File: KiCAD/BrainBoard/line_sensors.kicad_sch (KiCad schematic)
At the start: 0 parts

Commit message: feat: Line sensor thing push
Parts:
- added J6, J7, J8, J9: Conn_01x03_Socket, Connector_PinSocket_2.54mm:PinSocket_1x03_P2.54mm_Vertical, symbol Connector:Conn_01x03_Socket
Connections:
- new net 3V3: J6.2 (Pin_2), J7.2 (Pin_2), J8.2 (Pin_2), J9.2 (Pin_2)
- new net GND: J6.3 (Pin_3), J7.3 (Pin_3), J8.3 (Pin_3), J9.3 (Pin_3)
- new net LINE_1: J6.1 (Pin_1)
- new net LINE_2: J7.1 (Pin_1)
- new net LINE_3: J8.1 (Pin_1)
- new net LINE_4: J9.1 (Pin_1)

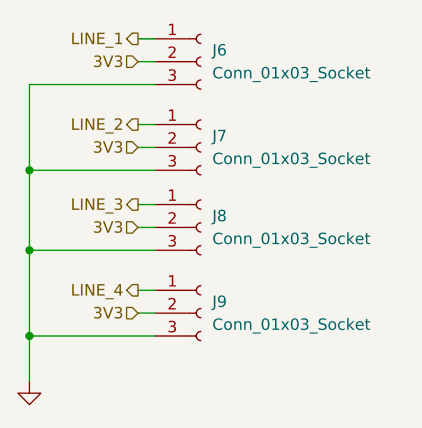
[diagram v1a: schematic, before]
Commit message: feat: add +5V line
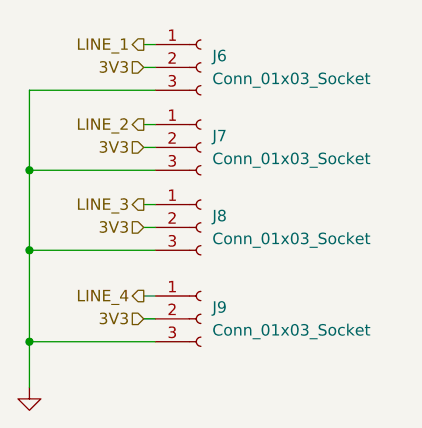
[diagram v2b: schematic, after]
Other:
- moved on the sheet: J6, J9
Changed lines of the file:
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@@
 	)
 	(junction
-		(at 139.7 121.285)
+		(at 139.7 121.92)
 		(diameter 0)
 		(color 0 0 0 0)
@@
 	(wire
 		(pts
-			(xy 151.765 116.205) (xy 153.67 116.205)
-		)
-		(stroke
-			(width 0)
-			(type default)
-		)
-	)
-	(wire
-		(pts
-			(xy 151.765 109.22) (xy 153.67 109.22)
-		)
-		(stroke
-			(width 0)
-			(type default)
-		)
-	)
-	(wire
-		(pts
-			(xy 151.765 88.265) (xy 153.67 88.265)
-		)
-		(stroke
-			(width 0)
-			(type default)
-		)
-	)
-	(wire
-		(pts
-			(xy 151.765 97.79) (xy 153.67 97.79)
-		)
-		(stroke
-			(width 0)
-			(type default)
-		)
-	)
-	(wire
-		(pts
-			(xy 151.765 118.745) (xy 153.67 118.745)
+			(xy 152.4 116.84) (xy 153.67 116.84)
+		)
+		(stroke
+			(width 0)
+			(type default)
+		)
+	)
+	(wire
+		(pts
+			(xy 152.4 109.22) (xy 153.67 109.22)
+		)
+		(stroke
+			(width 0)
+			(type default)
+		)
+	)
+	(wire
+		(pts
+			(xy 152.4 88.9) (xy 153.67 88.9)
+		)
+		(stroke
+			(width 0)
+			(type default)
+		)
+	)
+	(wire
+		(pts
+			(xy 152.4 97.79) (xy 153.67 97.79)
+		)
+		(stroke
+			(width 0)
+			(type default)
+		)
+	)
+	(wire
+		(pts
+			(xy 152.4 119.38) (xy 153.67 119.38)
 		)
 		(stroke
@@
 	(wire
 		(pts
-			(xy 151.765 100.33) (xy 153.67 100.33)
-		)
-		(stroke
-			(width 0)
-			(type default)
-		)
-	)
-	(wire
-		(pts
-			(xy 139.7 121.285) (xy 139.7 126.365)
-		)
-		(stroke
-			(width 0)
-			(type default)
-		)
-	)
-	(wire
-		(pts
-			(xy 151.765 106.68) (xy 153.67 106.68)
-		)
-		(stroke
-			(width 0)
-			(type default)
-		)
-	)
-	(wire
-		(pts
-			(xy 151.765 90.805) (xy 153.67 90.805)
-		)
-		(stroke
-			(width 0)
-			(type default)
-		)
-	)
-	(wire
-		(pts
-			(xy 139.7 111.76) (xy 139.7 121.285)
-		)
-		(stroke
-			(width 0)
-			(type default)
-		)
-	)
-	(wire
-		(pts
-			(xy 153.67 93.345) (xy 139.7 93.345)
+			(xy 152.4 100.33) (xy 153.67 100.33)
+		)
+		(stroke
+			(width 0)
+			(type default)
+		)
+	)
+	(wire
+		(pts
+			(xy 139.7 121.92) (xy 139.7 127)
+		)
+		(stroke
+			(width 0)
+			(type default)
+		)
+	)
+	(wire
+		(pts
+			(xy 152.4 106.68) (xy 153.67 106.68)
+		)
+		(stroke
+			(width 0)
+			(type default)
+		)
+	)
+	(wire
+		(pts
+			(xy 152.4 91.44) (xy 153.67 91.44)
+		)
+		(stroke
+			(width 0)
+			(type default)
+		)
+	)
+	(wire
+		(pts
+			(xy 139.7 111.76) (xy 139.7 121.92)
+		)
+		(stroke
+			(width 0)
+			(type default)
+		)
+	)
+	(wire
+		(pts
+			(xy 153.67 93.98) (xy 139.7 93.98)
 		)
 		(stroke
@@
 	(wire
 		(pts
-			(xy 139.7 121.285) (xy 153.67 121.285)
+			(xy 139.7 121.92) (xy 153.67 121.92)
 		)
 		(stroke
@@
 	(wire
 		(pts
-			(xy 139.7 93.345) (xy 139.7 102.87)
+			(xy 139.7 93.98) (xy 139.7 102.87)
 		)
 		(stroke
@@
 	(hierarchical_label "LINE_2"
 		(shape output)
-		(at 151.765 97.79 180)
+		(at 152.4 97.79 180)
 		(effects
 			(font
@@
 	(hierarchical_label "LINE_3"
 		(shape output)
-		(at 151.765 106.68 180)
+		(at 152.4 106.68 180)
 		(effects
 			(font
@@
 	(hierarchical_label "3V3"
 		(shape input)
-		(at 151.765 100.33 180)
+		(at 152.4 100.33 180)
 		(effects
 			(font
@@
 	(hierarchical_label "LINE_4"
 		(shape output)
-		(at 151.765 116.205 180)
+		(at 152.4 116.84 180)
 		(effects
 			(font
@@
 	(hierarchical_label "LINE_1"
 		(shape output)
-		(at 151.765 88.265 180)
+		(at 152.4 88.9 180)
 		(effects
 			(font
@@
 	(hierarchical_label "3V3"
 		(shape input)
-		(at 151.765 118.745 180)
+		(at 152.4 119.38 180)
 		(effects
 			(font
@@
 	(hierarchical_label "3V3"
 		(shape input)
-		(at 151.765 109.22 180)
+		(at 152.4 109.22 180)
 		(effects
 			(font
@@
 	(hierarchical_label "3V3"
 		(shape input)
-		(at 151.765 90.805 180)
+		(at 152.4 91.44 180)
 		(effects
 			(font
@@
 	(symbol
 		(lib_id "Connector:Conn_01x03_Socket")
-		(at 158.75 90.805 0)
+		(at 158.75 91.44 0)
 		(unit 1)
 		(exclude_from_sim no)
@@
 		(fields_autoplaced yes)
 		(property "Reference" "J6"
-			(at 160.02 89.5349 0)
+			(at 160.02 90.1699 0)
 			(effects
 				(font
@@
 		)
 		(property "Value" "Conn_01x03_Socket"
-			(at 160.02 92.0749 0)
+			(at 160.02 92.7099 0)
 			(effects
 				(font
@@
 		)
 		(property "Footprint" "Connector_PinSocket_2.54mm:PinSocket_1x03_P2.54mm_Vertical"
-			(at 158.75 90.805 0)
+			(at 158.75 91.44 0)
 			(effects
 				(font
@@
 		)
 		(property "Datasheet" "~"
-			(at 158.75 90.805 0)
+			(at 158.75 91.44 0)
 			(effects
 				(font
@@
 		)
 		(property "Description" "Generic connector, single row, 01x03, script generated"
-			(at 158.75 90.805 0)
+			(at 158.75 91.44 0)
 			(effects
 				(font
@@
 	(symbol
 		(lib_id "Connector:Conn_01x03_Socket")
-		(at 158.75 118.745 0)
+		(at 158.75 119.38 0)
 		(unit 1)
 		(exclude_from_sim no)
@@
 		(fields_autoplaced yes)
 		(property "Reference" "J9"
-			(at 160.02 117.4749 0)
+			(at 160.02 118.1099 0)
 			(effects
 				(font
@@
 		)
 		(property "Value" "Conn_01x03_Socket"
-			(at 160.02 120.0149 0)
+			(at 160.02 120.6499 0)
 			(effects
 				(font
@@
 		)
 		(property "Footprint" "Connector_PinSocket_2.54mm:PinSocket_1x03_P2.54mm_Vertical"
-			(at 158.75 118.745 0)
+			(at 158.75 119.38 0)
 			(effects
 				(font
@@
 		)
 		(property "Datasheet" "~"
-			(at 158.75 118.745 0)
+			(at 158.75 119.38 0)
 			(effects
 				(font
@@
 		)
 		(property "Description" "Generic connector, single row, 01x03, script generated"
-			(at 158.75 118.745 0)
+			(at 158.75 119.38 0)
 			(effects
 				(font
@@
 	(symbol
 		(lib_id "power:GND")
-		(at 139.7 126.365 0)
+		(at 139.7 127 0)
 		(unit 1)
 		(exclude_from_sim no)
@@
 		(fields_autoplaced yes)
 		(property "Reference" "#PWR030"
-			(at 139.7 132.715 0)
+			(at 139.7 133.35 0)
 			(effects
 				(font
@@
 		)
 		(property "Value" "GND"
-			(at 139.7 130.81 0)
+			(at 139.7 131.445 0)
 			(effects
 				(font
@@
 		)
 		(property "Footprint" ""
-			(at 139.7 126.365 0)
+			(at 139.7 127 0)
 			(effects
 				(font
@@
 		)
 		(property "Datasheet" ""
-			(at 139.7 126.365 0)
+			(at 139.7 127 0)
 			(effects
 				(font
@@
 		)
 		(property "Description" "Power symbol creates a global label with name \"GND\" , ground"
-			(at 139.7 126.365 0)
-			(effects
-				(font
+			(at 139.7 127 0)
+			(effects
+				(font
